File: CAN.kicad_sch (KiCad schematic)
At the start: 6 parts, among them CN2 WJ15EDGRC-3.81-2P, U7 ISO1050DWR

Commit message: 更新六层电机控制板设计与器件库
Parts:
- C36: footprint Capacitor_SMD:C_0402_1005Metric_Pad0.74x0.62mm_HandSolder -> Capacitor_SMD:C_0603_1608Metric_Pad1.08x0.95mm_HandSolder
- U7: footprint Package_SO:SOIC-16_3.9x9.9mm_P1.27mm -> Package_SO:SOIC-16W_7.5x10.3mm_P1.27mm
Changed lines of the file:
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@@
 			)
 		)
-		(property "Footprint" "Capacitor_SMD:C_0402_1005Metric_Pad0.74x0.62mm_HandSolder"
+		(property "Footprint" "Capacitor_SMD:C_0603_1608Metric_Pad1.08x0.95mm_HandSolder"
 			(at 102.87 100.33 0)
 			(hide yes)
@@
 			)
 		)
-		(property "Footprint" "Package_SO:SOIC-16_3.9x9.9mm_P1.27mm"
+		(property "Footprint" "Package_SO:SOIC-16W_7.5x10.3mm_P1.27mm"
 			(at 133.35 86.36 0)
 			(hide yes)

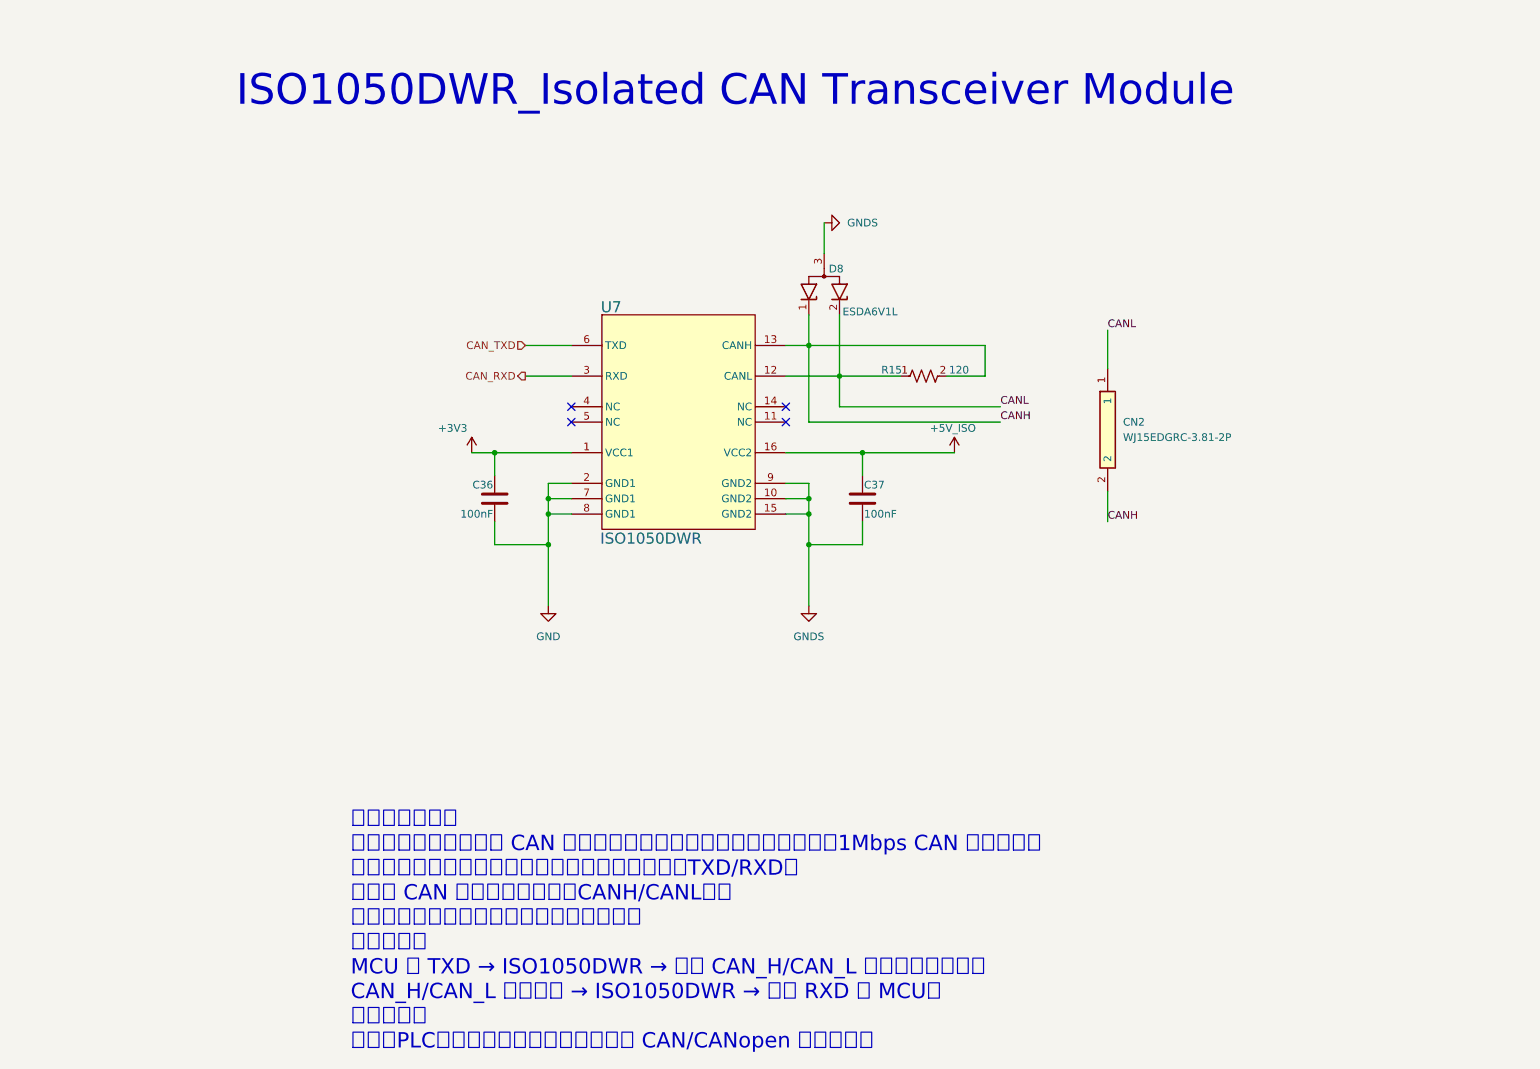
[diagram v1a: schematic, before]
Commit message: V2.0: sync KiCad design, add firmware snapshot and README
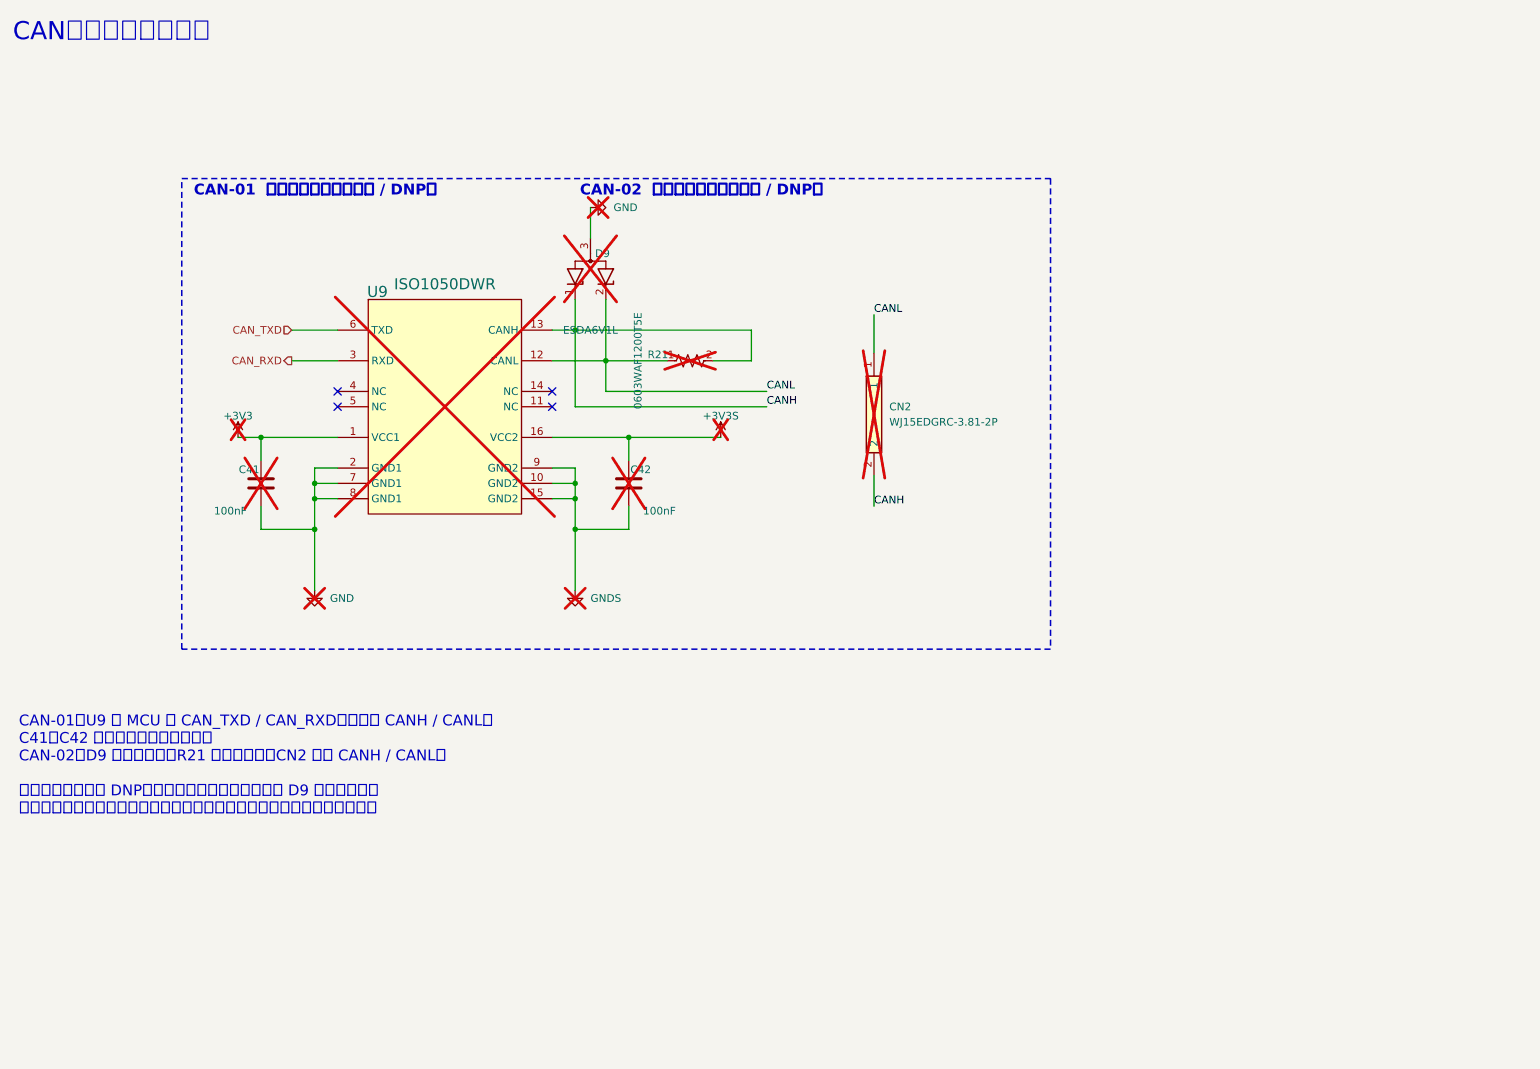
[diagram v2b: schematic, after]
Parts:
- C41: renamed from C36; footprint Capacitor_SMD:C_0603_1608Metric_Pad1.08x0.95mm_HandSolder -> Capacitor_SMD:C_0603_1608Metric; symbol CL05B104KB54PNC:CL05B104KB54PNC -> Project_Passives:CL10B104KB8NNNC_66bd0637; Capacitance (none) -> 100nF; Dielectric (none) -> X7R; MPN CL05B104KB54PNC -> CL10B104KB8NNNC; Manufacturer Samsung -> Samsung Electro-Mechanics; Tolerance (none) -> 10%; Voltage_Rating (none) -> 50V; application Automotive -> (none); grade AEC-Q200 -> (none); huaqiu_pn G4240447 -> (none); lead_free Yes -> (none); mount 表面贴装 -> (none); package 0402 -> 0603; packaging 4000pcs -> (none); tolerance 10 % -> (none); voltage_rating 50 V -> (none); now not fitted; now left out of the parts list
- C42: renamed from C37; footprint Capacitor_SMD:C_0402_1005Metric_Pad0.74x0.62mm_HandSolder -> Capacitor_SMD:C_0603_1608Metric; symbol CL05B104KB54PNC:CL05B104KB54PNC -> Project_Passives:CL10B104KB8NNNC_66bd0637; Capacitance (none) -> 100nF; Dielectric (none) -> X7R; MPN CL05B104KB54PNC -> CL10B104KB8NNNC; Manufacturer Samsung -> Samsung Electro-Mechanics; Tolerance (none) -> 10%; Voltage_Rating (none) -> 50V; application Automotive -> (none); grade AEC-Q200 -> (none); huaqiu_pn G4240447 -> (none); lead_free Yes -> (none); mount 表面贴装 -> (none); package 0402 -> 0603; packaging 4000pcs -> (none); tolerance 10 % -> (none); voltage_rating 50 V -> (none); now not fitted; now left out of the parts list
- CN2: now not fitted; now left out of the parts list
- D9: renamed from D8; footprint Package_TO_SOT_SMD:SOT-23-3 -> kicad_api_lib:ESDA6V1L; now not fitted; now left out of the parts list
- R21: renamed from R15; value 120 -> 0603WAF1200T5E; footprint Resistor_SMD:R_0603_1608Metric_Pad0.98x0.95mm_HandSolder -> Resistor_SMD:R_0603_1608Metric; now not fitted; now left out of the parts list
- U9: renamed from U7; footprint Package_SO:SOIC-16W_7.5x10.3mm_P1.27mm -> kicad_api_lib:ISO1050DWR; now not fitted; now left out of the parts list
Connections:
- net GND: now also D9.3 (A)
- net GNDS: no longer D9.3 (A)
- net +5V_ISO renamed +3V3S
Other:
- note added: "CAN-01 逻辑侧与收发器【备用 / DNP】"
- note added: "CAN-01：U9 接 MCU 的 CAN_TXD / CAN_RXD，转换为 CANH / CANL。 C41、C42 分别对应两侧电源去耦。 CAN-02：D9 为总线防护；R21 为端接电阻；CN2 引出 CANH / CANL。 本页器件当前均为 DNP。启用前需复核总线侧电压与 D9 的接地归属， 并确认隔离电源和地的边界；不能仅凭隔离芯片型号认定整板已实现隔离。"
- note added: "CAN-02 总线保护与端接【备用 / DNP】"
- note added: "CAN｜备用不装配接口"
- note removed: "ISO1050DWR_Isolated CAN Transceiver Module"
- note removed: "模块电路功能： 这是一个带隔离功能的 CAN 总线收发器电路，采用半双工，最高支持1Mbps CAN 通信速率； 该电路的主要功能是将微控制器的逻辑电平信号（TXD/RXD） 转换为 CAN 总线的差分信号（CANH/CANL）， 同时在逻辑侧和总线侧之间提供电气隔离。 引脚功能： MCU 的 TXD → ISO1050DWR → 驱动 CAN_H/CAN_L 差分信号上总线。 CAN_H/CAN_L 差分信号 → ISO1050DWR → 输出 RXD 给 MCU。 应用场景： 适用于PLC、伺服驱动器、工业机器人的 CAN/CANopen 通信隔离；"

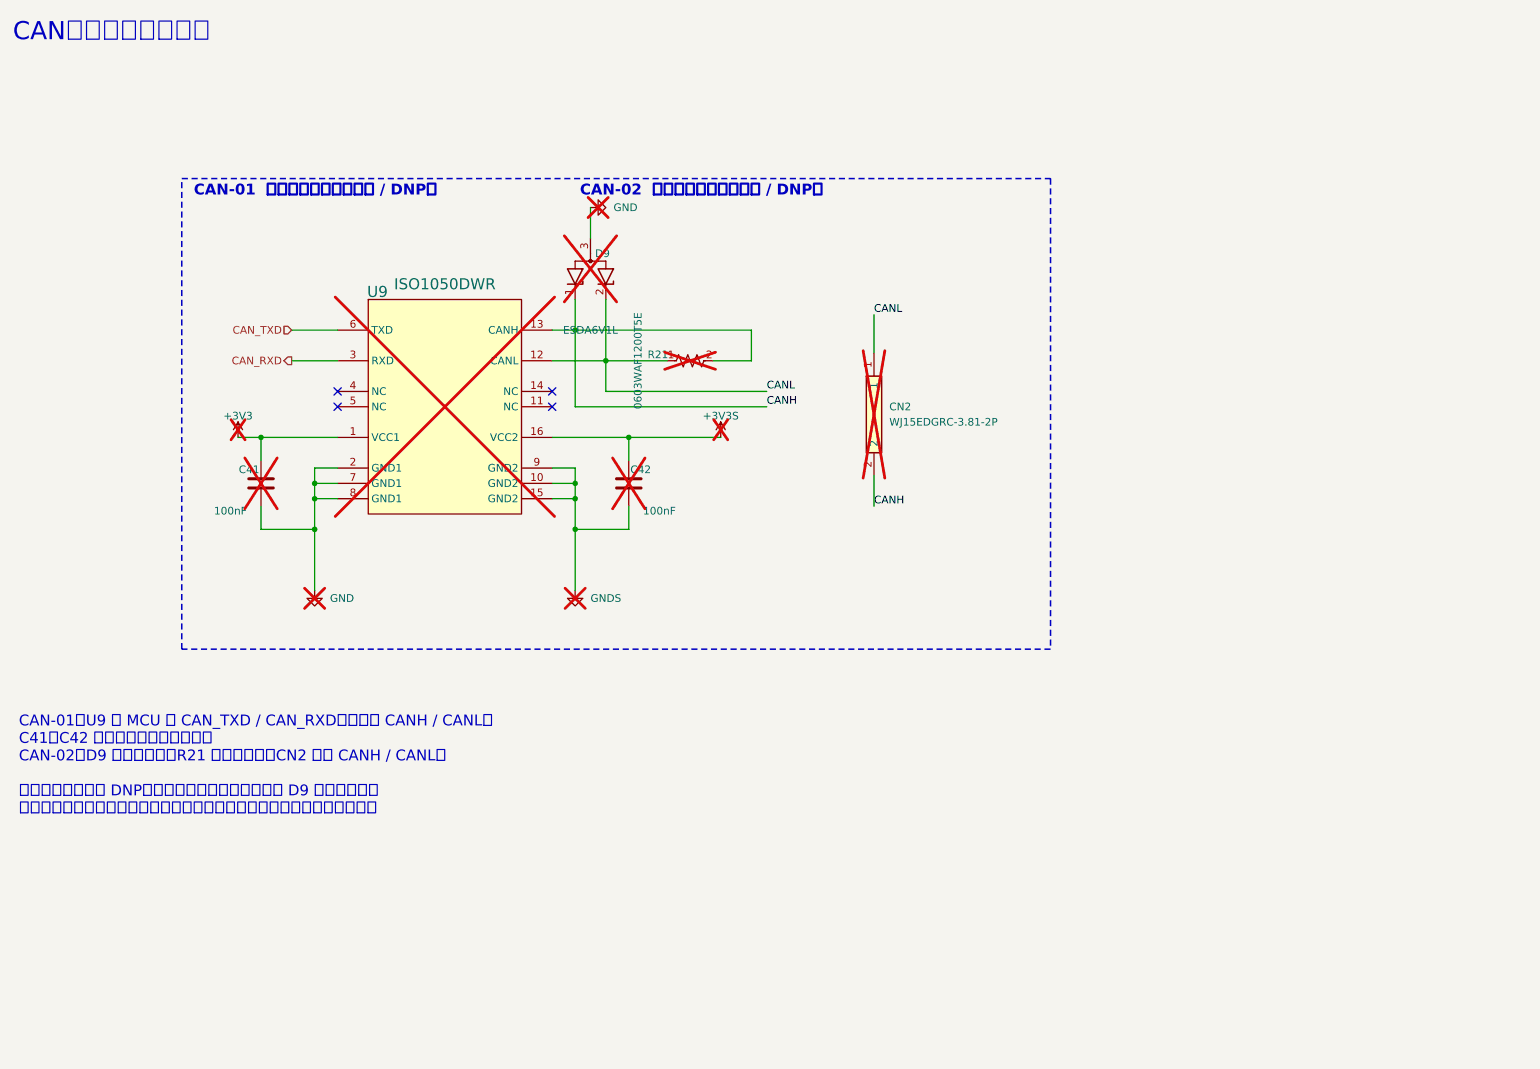
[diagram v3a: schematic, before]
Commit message: 更新V2.0电路设计及0.5oz内层制造交付资料
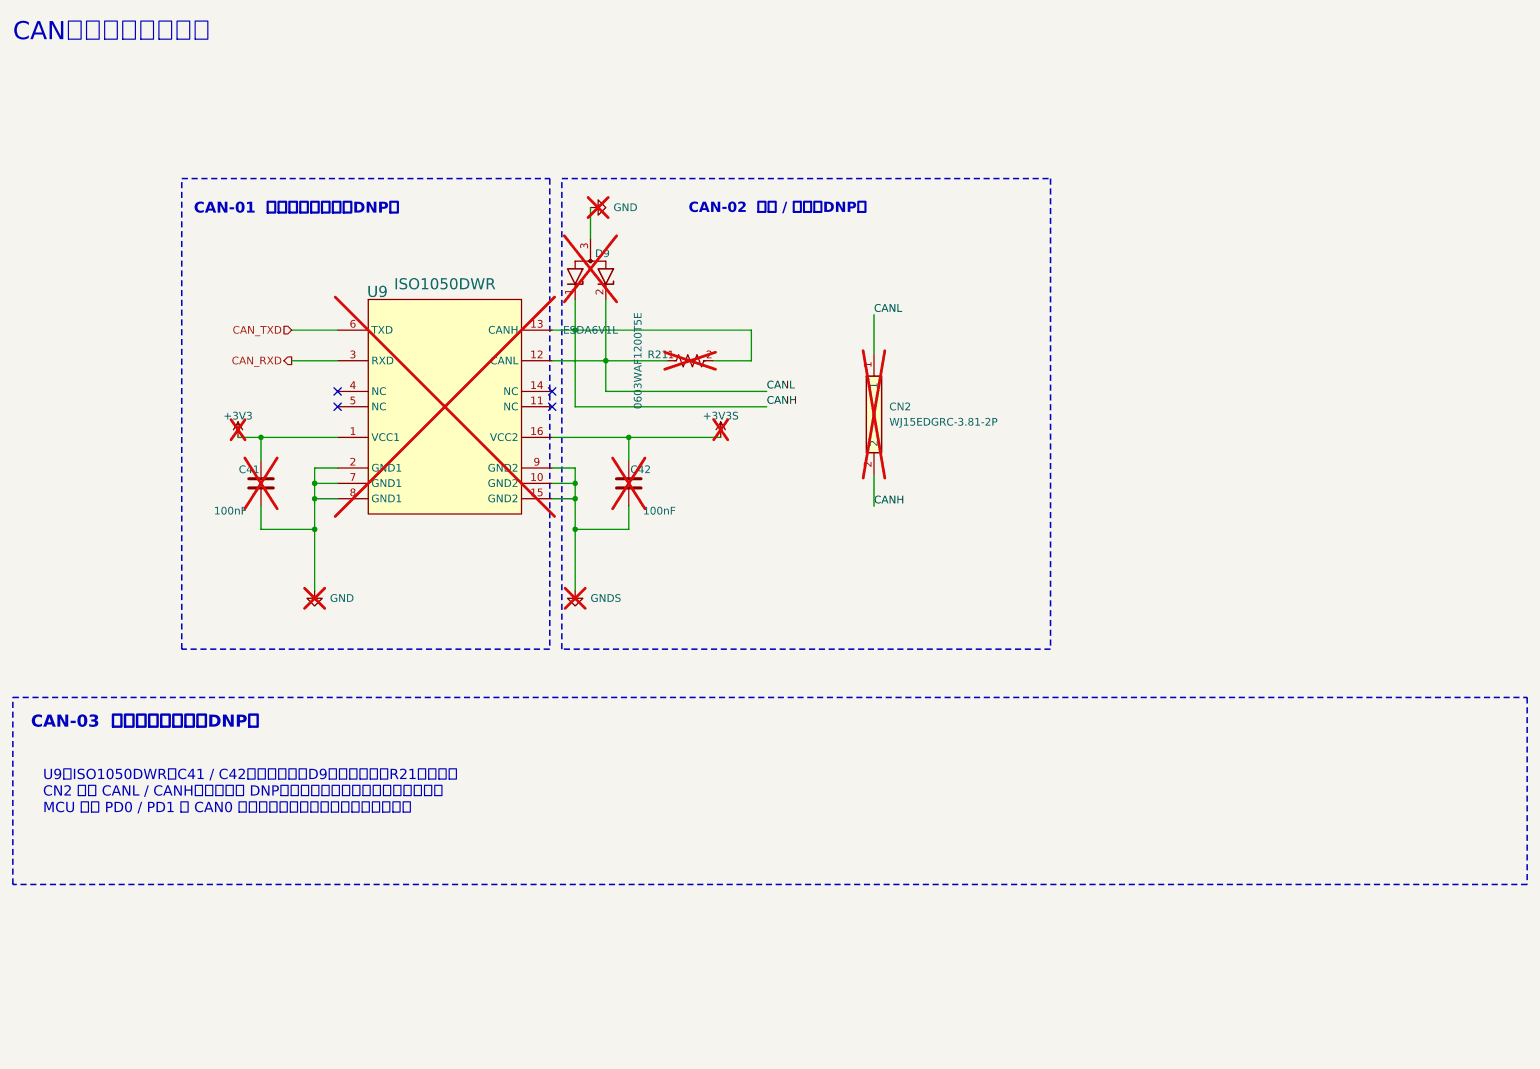
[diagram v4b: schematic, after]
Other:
- note added: "CAN-01 逻辑侧与收发器【DNP】"
- note added: "CAN-02 防护 / 端接【DNP】"
- note added: "CAN-03 功能与装配说明【DNP】"
- note added: "U9：ISO1050DWR；C41 / C42：两侧去耦；D9：总线防护；R21：端接。 CN2 引出 CANL / CANH。本页全部 DNP，启用前复核隔离电源与接地边界。 MCU 使用 PD0 / PD1 的 CAN0 重映射；分区框不代表电气隔离边界。"
- note removed: "CAN-01 逻辑侧与收发器【备用 / DNP】"
- note removed: "CAN-01：U9 接 MCU 的 CAN_TXD / CAN_RXD，转换为 CANH / CANL。 C41、C42 分别对应两侧电源去耦。 CAN-02：D9 为总线防护；R21 为端接电阻；CN2 引出 CANH / CANL。 本页器件当前均为 DNP。启用前需复核总线侧电压与 D9 的接地归属， 并确认隔离电源和地的边界；不能仅凭隔离芯片型号认定整板已实现隔离。"
- note removed: "CAN-02 总线保护与端接【备用 / DNP】"
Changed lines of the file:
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@@
 	(rectangle
 		(start 51 46)
+		(end 112 124)
+		(stroke
+			(width 0.254)
+			(type dash)
+		)
+		(fill
+			(type none)
+		)
+	)
+	(rectangle
+		(start 114 46)
 		(end 195 124)
 		(stroke
@@
 		)
 	)
+	(rectangle
+		(start 23 132)
+		(end 274 163)
+		(stroke
+			(width 0.254)
+			(type dash)
+		)
+		(fill
+			(type none)
+		)
+	)
+	(text "CAN-02  防护 / 端接【DNP】"
+		(exclude_from_sim no)
+		(at 135 50 0)
+		(effects
+			(font
+				(face "Microsoft YaHei")
+				(size 1.7 1.7)
+				(bold yes)
+			)
+			(justify left top)
+		)
+	)
 	(text "CAN｜备用不装配接口"
 		(exclude_from_sim no)
@@
 		(effects
 			(font
-				(face "宋体")
+				(face "Microsoft YaHei")
 				(size 3 3)
 			)
@@
 		)
 	)
-	(text "CAN-01  逻辑侧与收发器【备用 / DNP】"
+	(text "U9：ISO1050DWR；C41 / C42：两侧去耦；D9：总线防护；R21：端接。\nCN2 引出 CANL / CANH。本页全部 DNP，启用前复核隔离电源与接地边界。\nMCU 使用 PD0 / PD1 的 CAN0 重映射；分区框不代表电气隔离边界。"
 		(exclude_from_sim no)
-		(at 53 47 0)
+		(at 28 144 0)
 		(effects
 			(font
-				(face "宋体")
+				(face "Microsoft YaHei")
+				(size 1.7 1.7)
+			)
+			(justify left top)
+		)
+	)
+	(text "CAN-01  逻辑侧与收发器【DNP】"
+		(exclude_from_sim no)
+		(at 53 50 0)
+		(effects
+			(font
+				(face "Microsoft YaHei")
 				(size 1.8 1.8)
 				(bold yes)
@@
 		)
 	)
-	(text "CAN-02  总线保护与端接【备用 / DNP】"
+	(text "CAN-03  功能与装配说明【DNP】"
 		(exclude_from_sim no)
-		(at 117 47 0)
+		(at 26 135 0)
 		(effects
 			(font
-				(face "宋体")
-				(size 1.8 1.8)
+				(face "Microsoft YaHei")
+				(size 2 2)
 				(bold yes)
 			)
 			(justify left top)
-		)
-	)
-	(text "CAN-01：U9 接 MCU 的 CAN_TXD / CAN_RXD，转换为 CANH / CANL。\nC41、C42 分别对应两侧电源去耦。\nCAN-02：D9 为总线防护；R21 为端接电阻；CN2 引出 CANH / CANL。\n\n本页器件当前均为 DNP。启用前需复核总线侧电压与 D9 的接地归属，\n并确认隔离电源和地的边界；不能仅凭隔离芯片型号认定整板已实现隔离。"
-		(exclude_from_sim no)
-		(at 24 135 0)
-		(effects
-			(font
-				(face "宋体")
-				(size 1.8 1.8)
-			)
-			(justify left top)
